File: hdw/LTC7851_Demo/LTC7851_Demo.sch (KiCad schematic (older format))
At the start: 0 parts

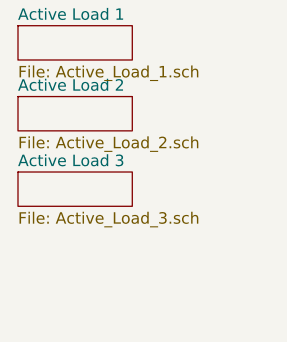
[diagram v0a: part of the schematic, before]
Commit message: Added active load sheets
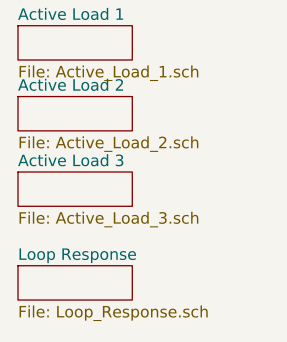
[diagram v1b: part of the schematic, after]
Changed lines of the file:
@@
 $Descr A 11000 8500
 encoding utf-8
-Sheet 1 13
+Sheet 1 15
 Title ""
 Date ""
@@
 F1 "Active_Load_3.sch" 50
 $EndSheet
+$Sheet
+S 3270 6180 500  150
+U 5BC30A46
+F0 "Loop Response" 50
+F1 "Loop_Response.sch" 50
+$EndSheet
 $EndSCHEMATC

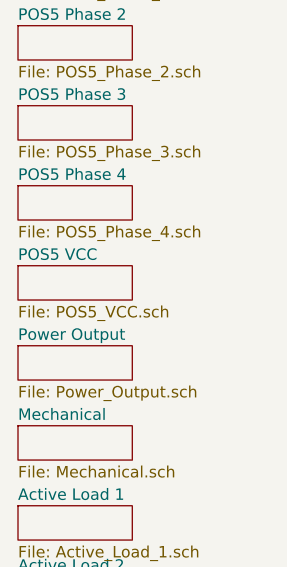
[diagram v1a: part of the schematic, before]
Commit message: Added component values for all phase 1 components
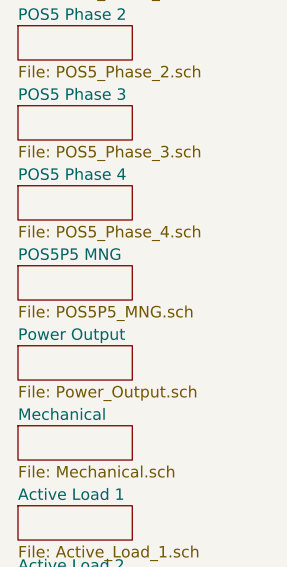
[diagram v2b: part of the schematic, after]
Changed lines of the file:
@@
 $Descr A 11000 8500
 encoding utf-8
-Sheet 1 15
+Sheet 1 14
 Title ""
 Date ""
@@
 S 3270 4080 500  150
 U 5BB9CE4B
-F0 "POS5 VCC" 50
-F1 "POS5_VCC.sch" 50
+F0 "POS5P5 MNG" 50
+F1 "POS5P5_MNG.sch" 50
 $EndSheet
 $Sheet

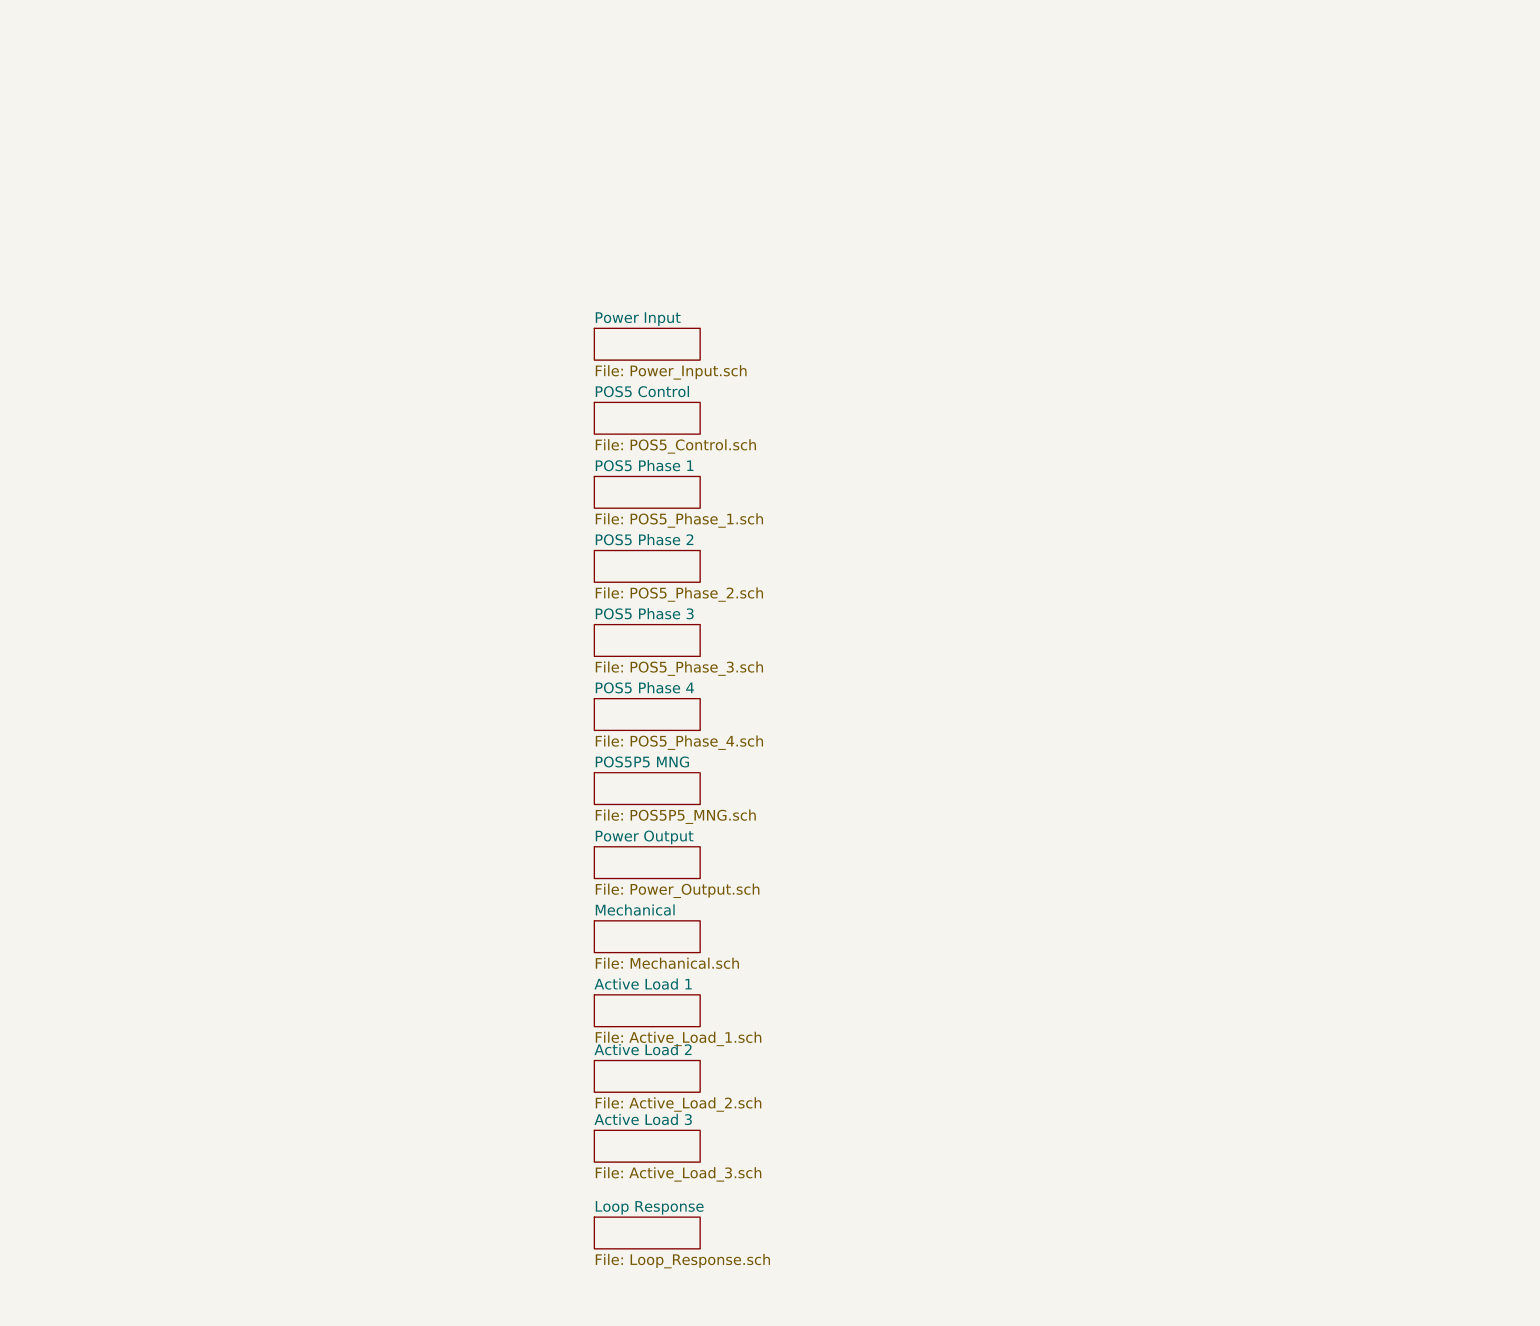
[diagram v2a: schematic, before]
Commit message: Added page titles
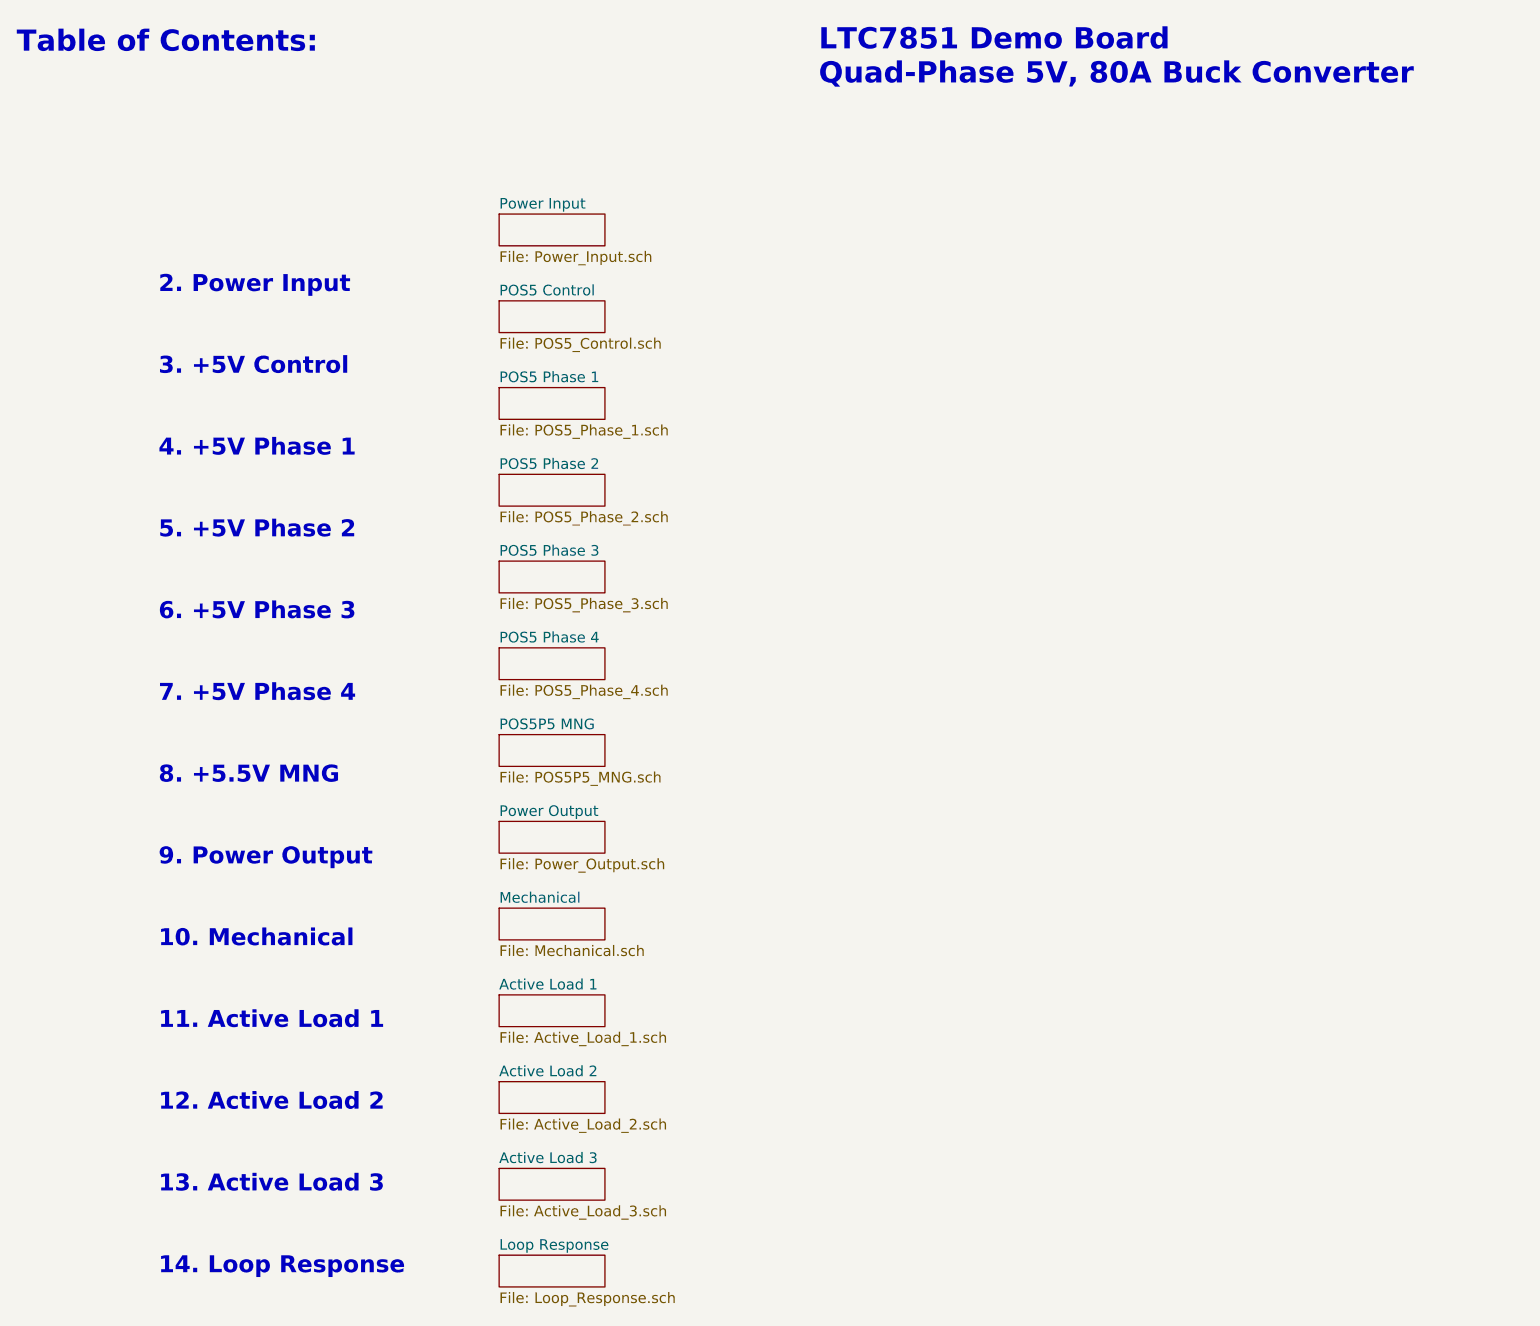
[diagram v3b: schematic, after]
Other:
- note added: "2. Power Input\n\n\n3. +5V Control\n\n\n4. +5V Phase 1\n\n\n5. +5V Phase 2\n\n\n6. +5V Phase 3\n\n\n7. +5V Phase 4\n\n\n8. +5.5V MNG\n\n\n9. Power Output\n\n\n10. Mechanical\n\n\n11. Active Load 1\n\n\n12. Active Load 2\n\n\n13. Active Load 3\n\n\n14. Loop Response"
- note added: "LTC7851 Demo Board\nQuad-Phase 5V, 80A Buck Converter"
- note added: "Table of Contents:"
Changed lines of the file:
@@
 $EndDescr
 $Sheet
-S 3270 1980 500  150
+S 2820 1440 500  150
 U 5BB86F23
 F0 "Power Input" 50
@@
 $EndSheet
 $Sheet
-S 3270 2330 500  150
+S 2820 1850 500  150
 U 5BB86F26
 F0 "POS5 Control" 50
@@
 $EndSheet
 $Sheet
-S 3270 2680 500  150
+S 2820 2260 500  150
 U 5BB86F29
 F0 "POS5 Phase 1" 50
@@
 $EndSheet
 $Sheet
-S 3270 3030 500  150
+S 2820 2670 500  150
 U 5BB86F2C
 F0 "POS5 Phase 2" 50
@@
 $EndSheet
 $Sheet
-S 3270 3380 500  150
+S 2820 3080 500  150
 U 5BB86F2F
 F0 "POS5 Phase 3" 50
@@
 $EndSheet
 $Sheet
-S 3270 3730 500  150
+S 2820 3490 500  150
 U 5BB86F32
 F0 "POS5 Phase 4" 50
@@
 $EndSheet
 $Sheet
-S 3270 4080 500  150
+S 2820 3900 500  150
 U 5BB9CE4B
 F0 "POS5P5 MNG" 50
@@
 $EndSheet
 $Sheet
-S 3270 4430 500  150
+S 2820 4310 500  150
 U 5BB9D026
 F0 "Power Output" 50
@@
 $EndSheet
 $Sheet
-S 3270 4780 500  150
+S 2820 4720 500  150
 U 5BB9D688
 F0 "Mechanical" 50
@@
 $EndSheet
 $Sheet
-S 3270 5130 500  150
+S 2820 5130 500  150
 U 5BBF20D5
 F0 "Active Load 1" 50
@@
 $EndSheet
 $Sheet
-S 3270 5440 500  150
+S 2820 5540 500  150
 U 5BBF20D8
 F0 "Active Load 2" 50
@@
 $EndSheet
 $Sheet
-S 3270 5770 500  150
+S 2820 5950 500  150
 U 5BBF20DB
 F0 "Active Load 3" 50
@@
 $EndSheet
 $Sheet
-S 3270 6180 500  150
+S 2820 6360 500  150
 U 5BC30A46
 F0 "Loop Response" 50
 F1 "Loop_Response.sch" 50
 $EndSheet
+Text Notes 540  690  0    100  ~ 20
+Table of Contents:
+Text Notes 4330 840  0    100  ~ 20
+LTC7851 Demo Board\nQuad-Phase 5V, 80A Buck Converter
+Text Notes 1210 6460 0    80   ~ 16
+2. Power Input\n\n\n3. +5V Control\n\n\n4. +5V Phase 1\n\n\n5. +5V Phase 2\n\n\n6. +5V Phase 3\n\n\n7. +5V Phase 4\n\n\n8. +5.5V MNG\n\n\n9. Power Output\n\n\n10. Mechanical\n\n\n11. Active Load 1\n\n\n12. Active Load 2\n\n\n13. Active Load 3\n\n\n14. Loop Response
 $EndSCHEMATC
